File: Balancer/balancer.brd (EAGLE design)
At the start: 139.7 x 325.1 mm, 323 parts, among them Q1 BSS123W, Q10A SIR882DP-T1-GE3, Q10B SIS468DN-T1-GE3, Q11A SIR882DP-T1-GE3, Q11B SIS468DN-T1-GE3, Q12A SIR882DP-T1-GE3, Q12B SIS468DN-T1-GE3, Q1A8 SIR882DP-T1-GE3, Q1B8 SIS468DN-T1-GE3, Q2 BSS123W, Q3A SIR882DP-T1-GE3, Q3B SIS468DN-T1-GE3, Q4 MMBT3906LT1G, Q4A SIR882DP-T1-GE3, Q4B SIS468DN-T1-GE3, Q5 FDN5618P, Q5A SIR882DP-T1-GE3, Q5B SIS468DN-T1-GE3, Q6 CMPT3904E_TR_PBFREE, Q6A SIR882DP-T1-GE3, Q6B SIS468DN-T1-GE3, Q9A SIR882DP-T1-GE3, Q9B SIS468DN-T1-GE3, T10 750312504, T11 750312504, T12 750312504, T3 750312504, T4 750312504, T5 750312504, T6 750312504, T8 750312504, T9 750312504, U1 LTC3300ILXE-1PBF, U2 LTC3300ILXE-1PBF

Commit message: update1
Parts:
- moved F14 275.9 mm to (118.1, 309.9), flipped to the bottom, turned to 90 degrees
- moved F12 253.0 mm to (130.8, 288.3), flipped to the bottom
- moved D12E 243.4 mm to (119.4, 280.7), flipped to the bottom, turned to 90 degrees
- moved F11 228.1 mm to (130.8, 265.4), flipped to the bottom
- moved D11E 227.1 mm to (119.4, 262.9), flipped to the bottom, turned to 90 degrees
- moved D10E 211.2 mm to (119.4, 242.6), flipped to the bottom, turned to 90 degrees
- moved F10 202.1 mm to (130.8, 241.3), flipped to the bottom
- moved D9E 196.6 mm to (119.4, 221.0), flipped to the bottom, turned to 90 degrees
- moved C13 179.3 mm to (118.1, 170.2), flipped to the bottom
- moved D6E 173.9 mm to (119.4, 180.3), flipped to the bottom, turned to 90 degrees
- moved F9 171.2 mm to (109.2, 217.2), flipped to the bottom
- moved D5E 166.0 mm to (119.4, 161.3), flipped to the bottom, turned to 90 degrees
- moved D4E 159.9 mm to (119.4, 144.8), flipped to the bottom, turned to 90 degrees
- moved D3E 155.7 mm to (119.4, 127.0), flipped to the bottom, turned to 90 degrees
- moved C16 146.0 mm to (38.1, 255.3), flipped to the bottom
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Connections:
- removed net CTRL: U1.15
- net V-: now also U1.15

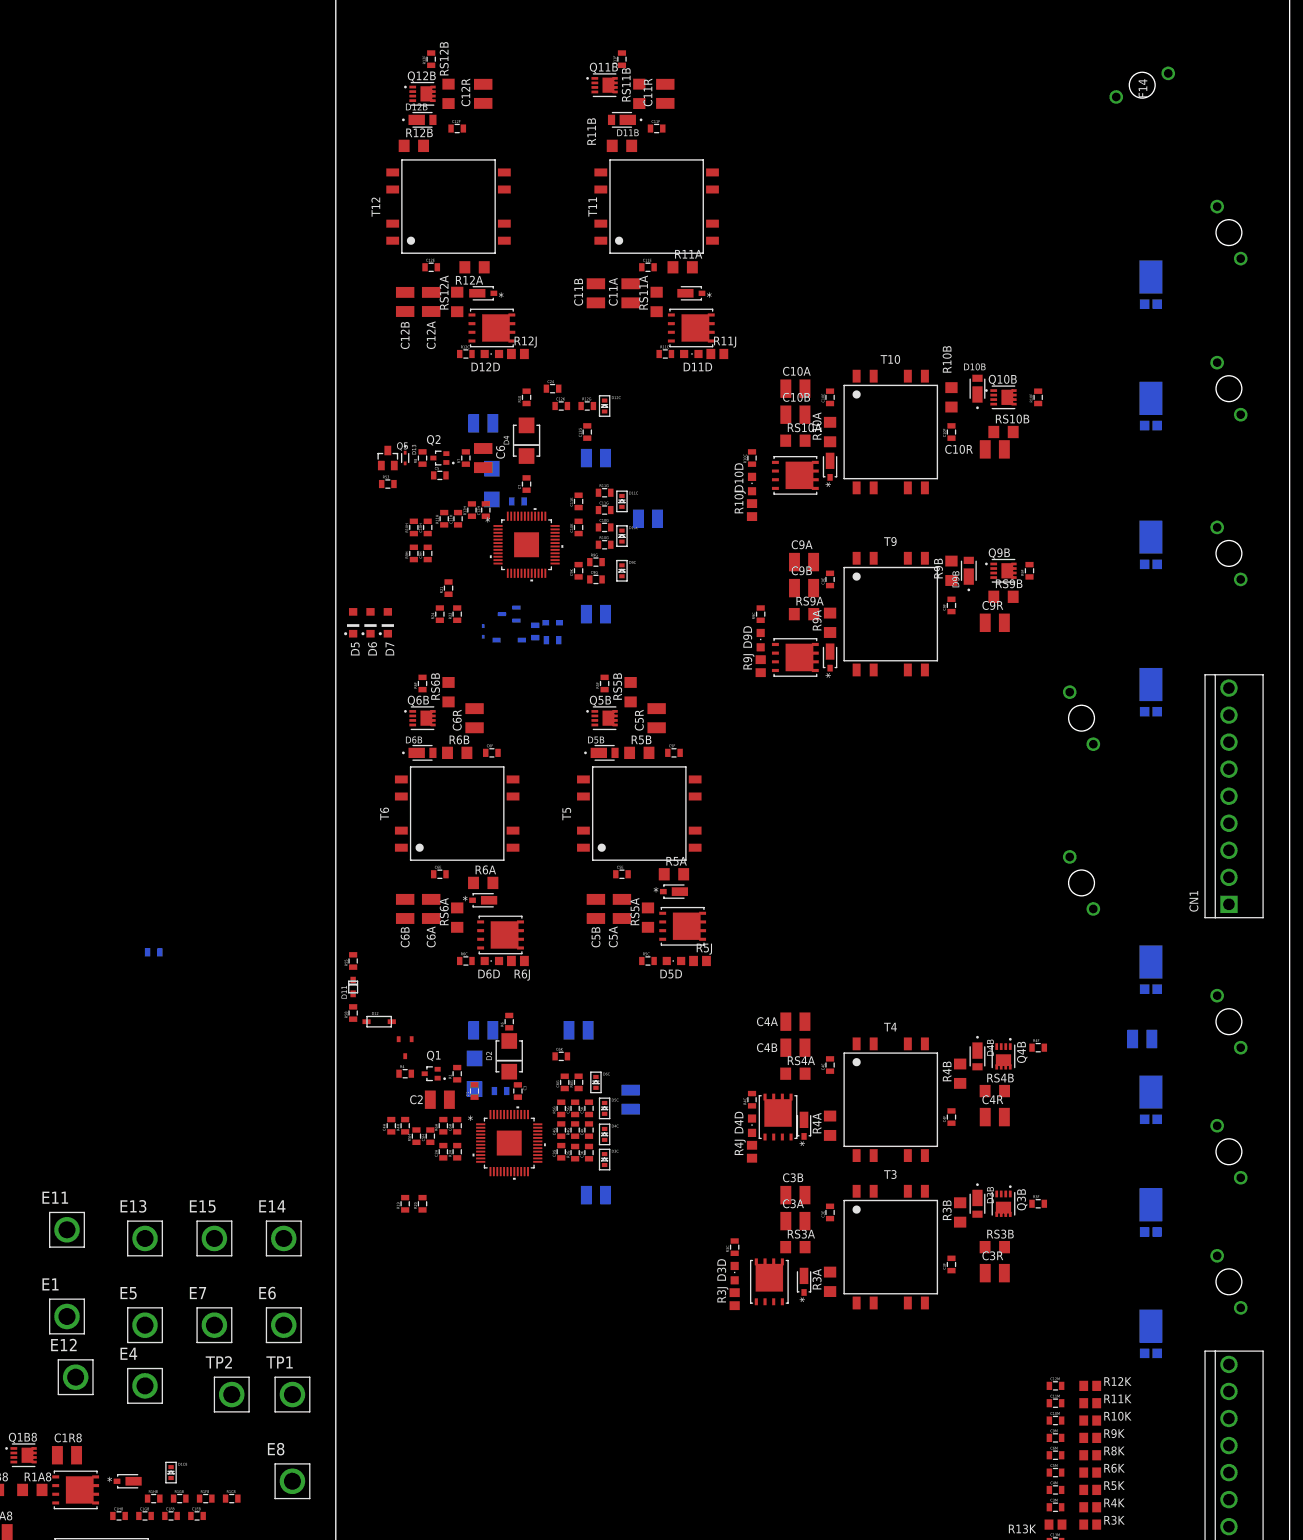
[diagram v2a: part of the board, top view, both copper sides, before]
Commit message: removed R5 & placed all component on PCB
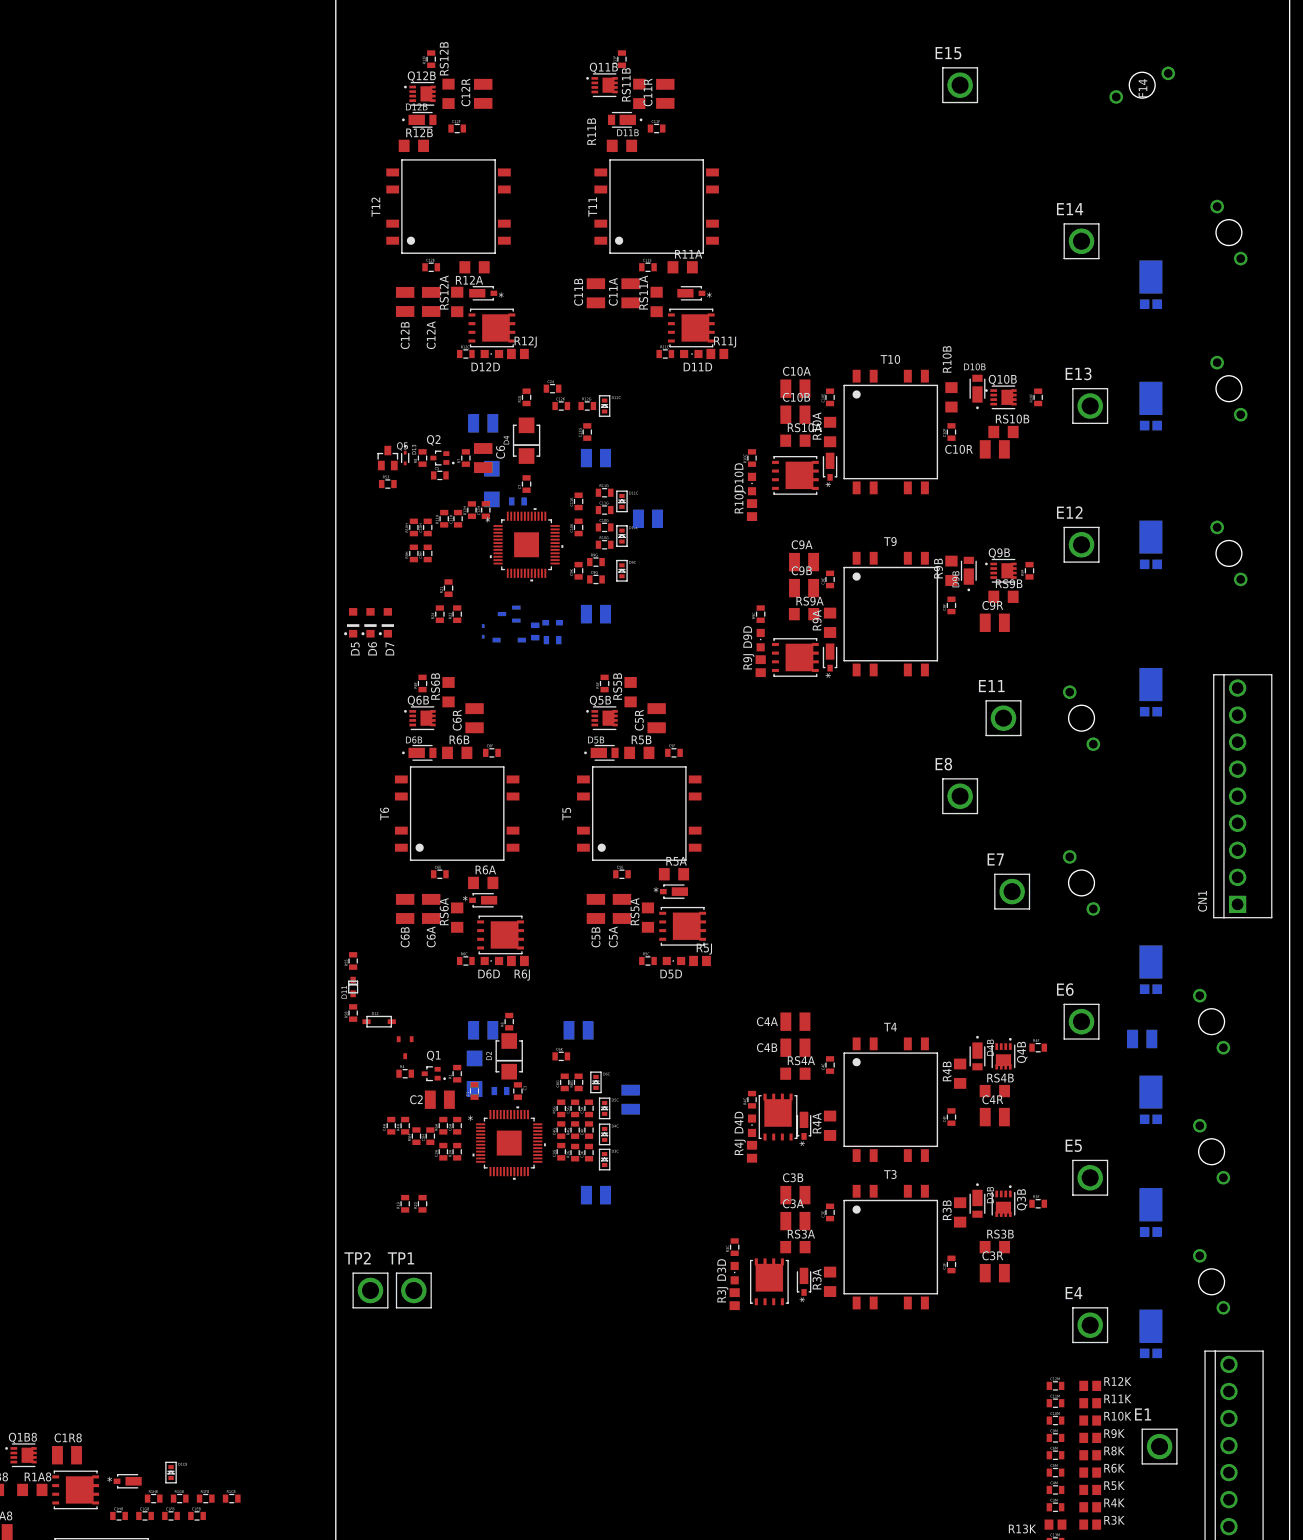
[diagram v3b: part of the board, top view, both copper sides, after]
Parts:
- removed R5: 0 ohm, Ilya_Teach:0805
- moved E15 201.1 mm to (91.4, 309.9)
- moved E12 191.2 mm to (109.2, 242.6)
- moved E14 187.0 mm to (109.2, 287.0)
- moved E13 184.5 mm to (110.5, 262.9)
- moved E1 161.1 mm to (120.7, 110.5)
- moved E11 156.3 mm to (97.8, 217.2)
- moved E5 140.1 mm to (110.5, 149.9)
- moved E8 140.1 mm to (91.4, 205.7)
- moved E4 138.7 mm to (110.5, 128.3)
- moved E7 133.0 mm to (99.1, 191.8)
- moved E6 125.0 mm to (109.2, 172.7)
- moved TP2 25.4 mm to (5.08, 133.3)
- moved TP1 23.4 mm to (11.4, 133.3)
- moved F3 2.54 mm to (128.3, 134.6)
- moved F4 2.54 mm to (128.3, 153.7)
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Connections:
- net BOOST+: no longer R5.2
- net N$1: no longer R5.1

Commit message: update
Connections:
- net N$109: now also Q11A.9
- net N$125: now also Q12A.9
- net N$141: now also Q1A8.9
- net N$15: now also Q3A.9
- net N$29: now also Q4A.9
- net N$45: now also Q5A.9
- net N$61: now also Q6A.9
- net N$77: now also Q9A.9
- net N$93: now also Q10A.9

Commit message: drew PCB
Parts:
- moved C10K 16.6 mm to (52.1, 243.8), turned to 270 degrees
- moved C9K 16.6 mm to (52.1, 237.5), turned to 270 degrees
- moved R12G 11.0 mm to (35.3, 252.0)
- moved C12G 9.89 mm to (34.2, 249.6), turned to 270 degrees
- moved D12C 8.89 mm to (37.8, 254.1)
- moved C11K 5.68 mm to (40.6, 251.5), turned to 270 degrees
- moved C12R 4.83 mm to (18.8, 304.7)
- moved C10G 3.81 mm to (39.4, 241.3)
- moved C11G 3.81 mm to (39.4, 243.8)
- moved C9G 3.81 mm to (38.1, 233.7)
- moved D10C 3.81 mm to (41.9, 240.0)
- moved D9C 3.81 mm to (41.9, 234.9)
- moved R10G 3.81 mm to (39.4, 238.8)
- moved R11G 3.81 mm to (39.4, 246.4)
- moved R9G 3.81 mm to (38.1, 236.2)
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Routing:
- net G12P: track 0.00 -> 13.0 mm, vias 0 -> 2
- net I12P: track 0.00 -> 6.76 mm
- net C12: track 0.00 -> 5.50 mm, vias 0 -> 8
- net N$135: track 0.00 -> 3.21 mm, vias 0 -> 1
- net N$152: track 0.00 -> 2.80 mm
- net N$53: track 0.00 -> 2.06 mm
- net N$46: track 0.00 -> 2.06 mm
- net N$127: track 0.00 -> 1.27 mm, vias 0 -> 2
- added copper zone on layer 1, net C11
- added copper zone on layer 1, net C12
- added copper zone on layer 1, net C6
- added copper zone on layer 1, net G12P
- added copper zone on layer 1, net G12S
- added copper zone on layer 1, net N$120
- added copper zone on layer 1, net N$123
- added copper zone on layer 1, net N$125
- added copper zone on layer 1, net N$127
- added copper zone on layer 1, net N$128
- added copper zone on layer 1, net N$129
- added copper zone on layer 1, net N$131
- added copper zone on layer 1, net N$132
- added copper zone on layer 1, net N$134
- added copper zone on layer 1, net N$42
- added copper zone on layer 1, net TOP6_TS

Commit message: made more changes on board
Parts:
- moved C10K 8.87 mm to (43.4, 241.8)
- moved Q10A 7.73 mm to (68.6, 260.4)
- moved C10R 7.73 mm to (97.8, 264.2)
- moved C10A 7.73 mm to (68.6, 273.1)
- moved C10B 7.73 mm to (68.6, 269.2)
- moved C10F 7.73 mm to (91.4, 266.7)
- moved D10A 7.73 mm to (73.7, 261.6)
- moved D10B 7.73 mm to (95.2, 273.1)
- moved R10A 7.73 mm to (73.7, 266.7)
- moved R10J 7.73 mm to (62.2, 255.3)
- moved RS10A 7.73 mm to (68.6, 265.4)
- moved RS10B 7.73 mm to (99.1, 266.7)
- moved T10 7.73 mm to (82.5, 266.7)
- moved D10D 7.73 mm to (62.2, 259.1)
- moved R10C 7.73 mm to (62.2, 262.9)
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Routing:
- net C11: track 0.00 -> 15.2 mm, vias 10 -> 18
- net G11P: track 0.00 -> 11.5 mm, vias 0 -> 1
- net G10P: track 0.00 -> 11.0 mm, vias 0 -> 1
- net I11P: track 0.00 -> 7.31 mm
- net I10P: track 0.00 -> 7.01 mm
- net N$95: track 0.00 -> 1.15 mm, vias 0 -> 1
- net N$111: track 0.00 -> 1.15 mm, vias 0 -> 2
- added copper zone on layer 1, net C10
- added copper zone on layer 1, net G11P
- added copper zone on layer 1, net G11S
- added copper zone on layer 1, net N$104
- added copper zone on layer 1, net N$107
- added copper zone on layer 1, net N$109
- added copper zone on layer 1, net N$111
- added copper zone on layer 1, net N$112
- added copper zone on layer 1, net N$113
- added copper zone on layer 1, net N$115
- added copper zone on layer 1, net N$116
- added copper zone on layer 1, net N$118
- added copper zone on layer 1, net N$41
- added copper zone on layer 1, net N$71

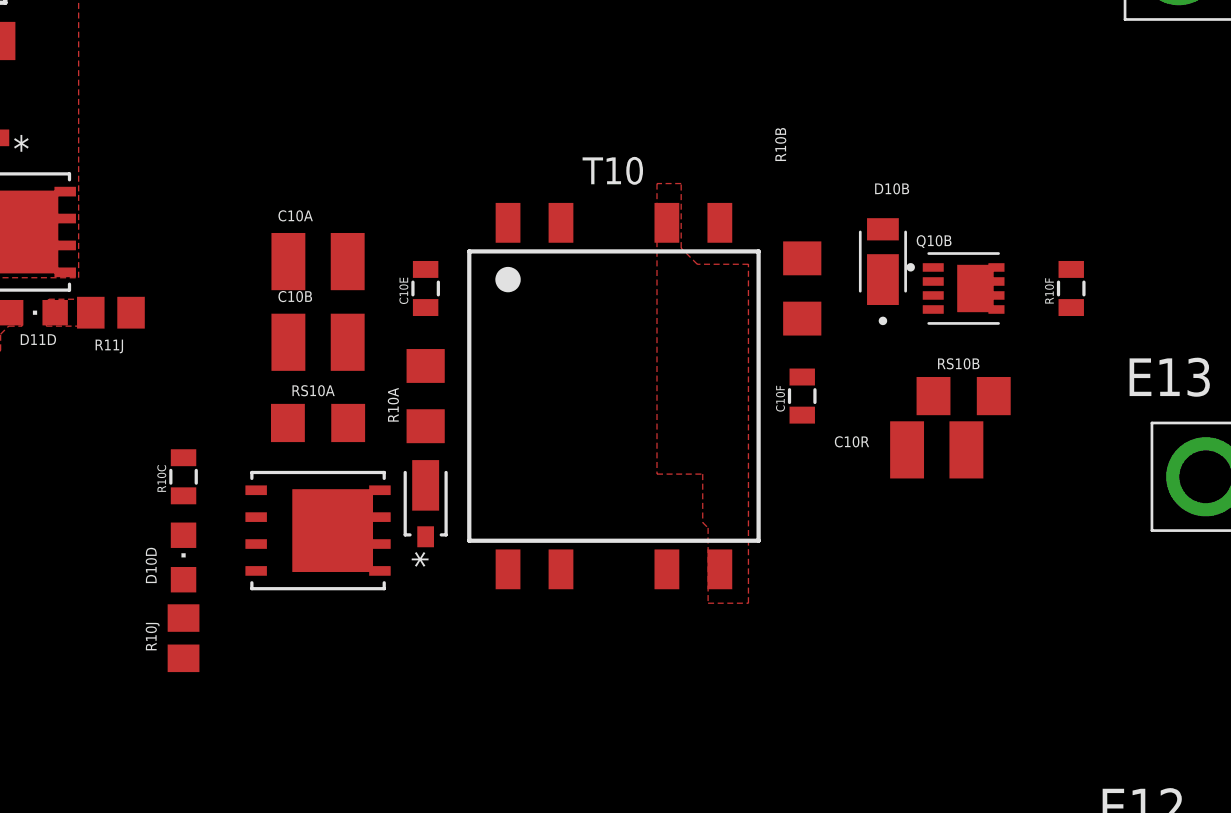
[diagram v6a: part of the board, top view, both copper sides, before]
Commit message: made more connections on pcb
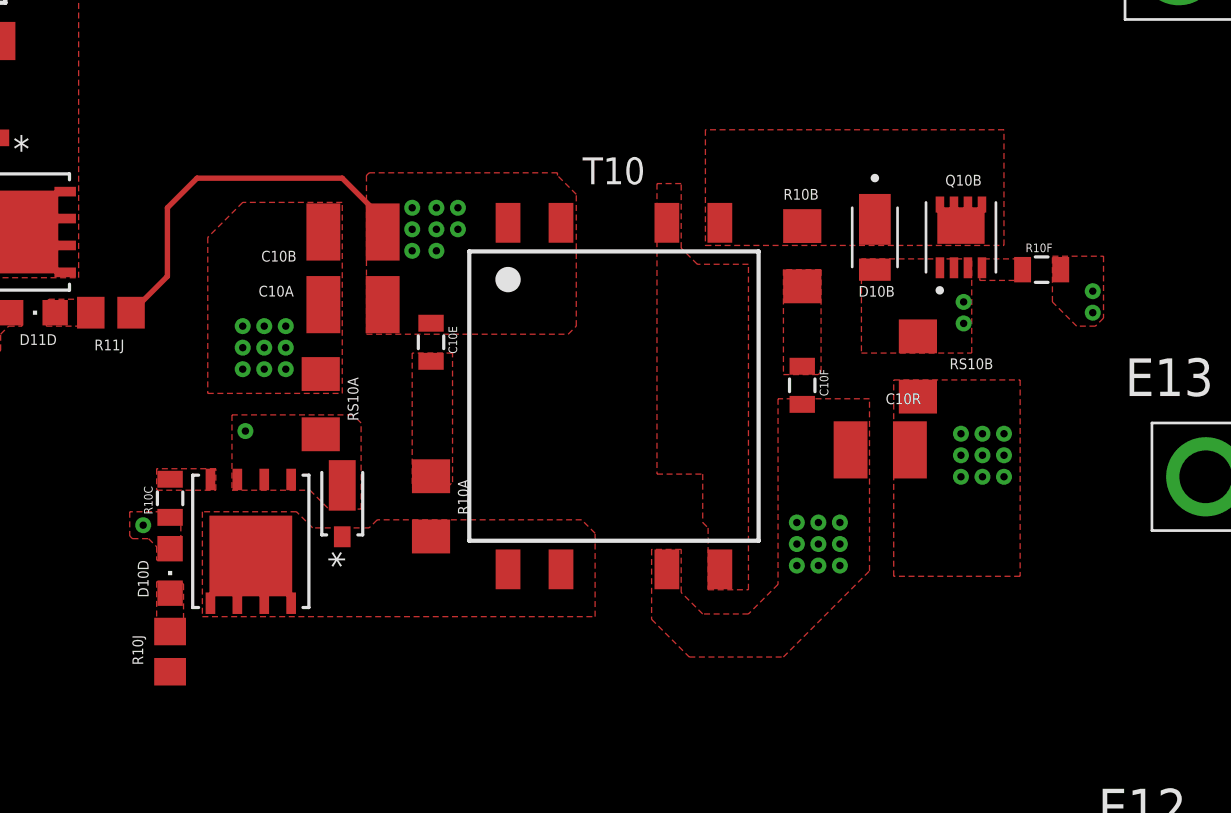
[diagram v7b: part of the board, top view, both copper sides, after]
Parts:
- moved R10A 5.21 mm to (73.9, 261.5), turned to 270 degrees
- moved D10A 3.94 mm to (69.7, 261.6)
- moved Q10A 3.22 mm to (65.4, 259.8), turned to 270 degrees
- moved C10R 2.67 mm to (95.1, 264.2), turned to 0 degrees
- moved RS10B 2.57 mm to (96.9, 268.1), turned to 90 degrees
- moved C10E 2.55 mm to (73.9, 269.2), turned to 270 degrees
- moved C10B 2.43 mm to (70.2, 271.0), turned to 180 degrees
- moved Q10B 2.42 mm to (98.9, 274.2), turned to 90 degrees
- moved C10A 2.16 mm to (70.2, 274.4), turned to 180 degrees
- moved R10F 1.66 mm to (102.7, 272.7), turned to 0 degrees
- moved R10B 1.52 mm to (91.4, 273.3)
- moved D10B 1.20 mm to (94.9, 274.2), turned to 270 degrees
- moved R10C 1.20 mm to (61.6, 261.9)
- moved R10J 0.90 mm to (61.6, 254.6)
- moved RS10A 0.90 mm to (68.7, 266.3), turned to 270 degrees
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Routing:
- net C10: track 0.00 -> 17.8 mm, vias 9 -> 17
- net N$95: vias 1 -> 2
- net G10P: vias 1 -> 2
- added copper zone on layer 1, net C9
- added copper zone on layer 1, net G10P
- added copper zone on layer 1, net G10S
- added copper zone on layer 1, net N$100
- added copper zone on layer 1, net N$102
- added copper zone on layer 1, net N$39
- added copper zone on layer 1, net N$88
- added copper zone on layer 1, net N$91
- added copper zone on layer 1, net N$93
- added copper zone on layer 1, net N$95
- added copper zone on layer 1, net N$96
- added copper zone on layer 1, net N$97
- added copper zone on layer 1, net N$99
- removed copper zone on layer 1, net N$71
